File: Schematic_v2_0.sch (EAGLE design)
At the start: 8 parts, among them IC1 MCP73831T-2ACI_OT, J1 692121030100

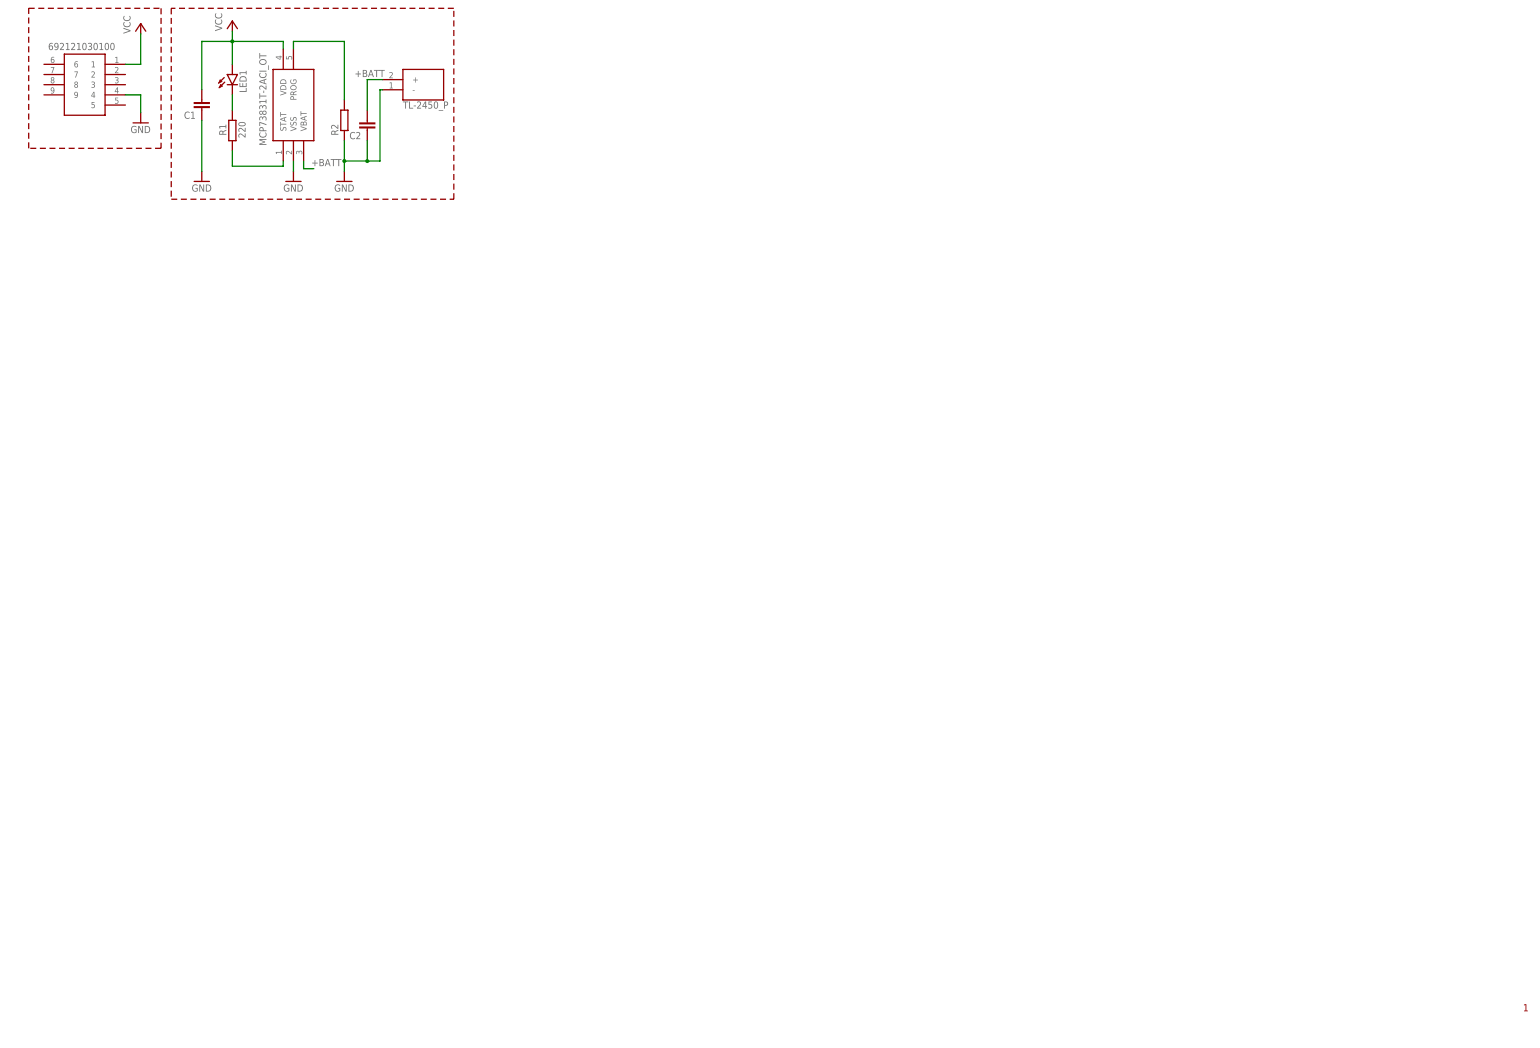
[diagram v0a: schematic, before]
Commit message: Se Agregro el bloque de carga de batería
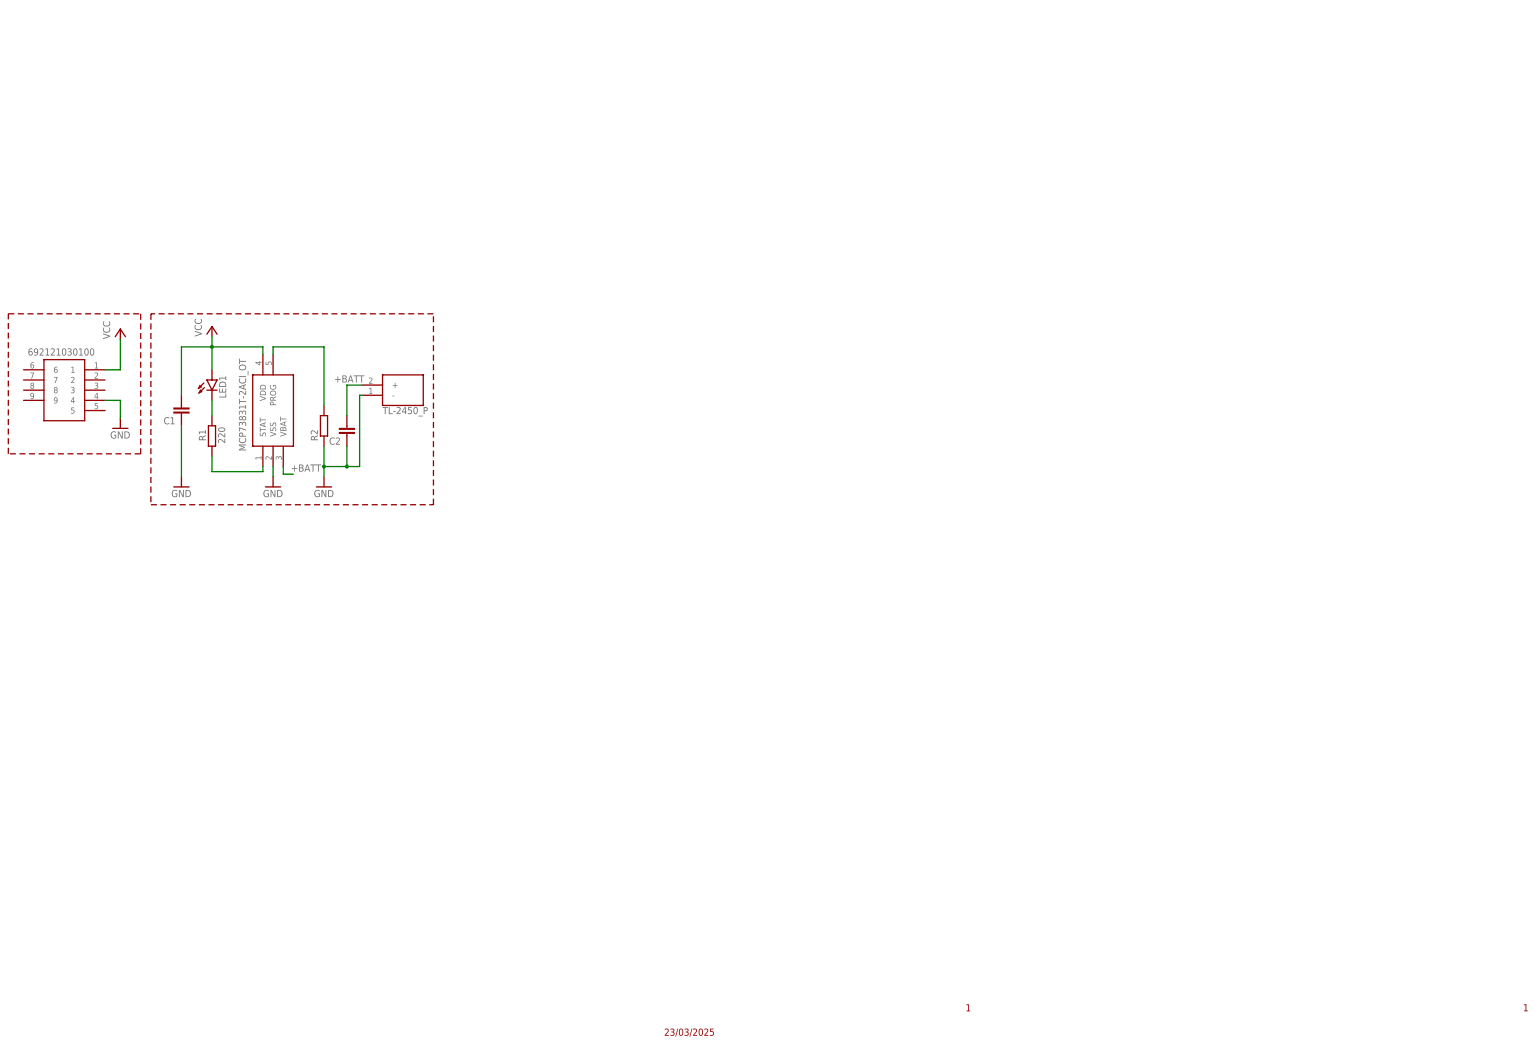
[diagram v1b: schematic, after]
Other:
- note added: "23/03/2025"
- moved on the sheet: C1, C2, LED1, R1, R2
